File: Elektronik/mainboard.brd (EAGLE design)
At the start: 27 x 27.4 mm, 35 parts, among them IC1 TXS0102DCU, IC2 SP6201EM5-L-3-3, IC3 SRV05-4.TCT, X2 USB-MINI32005-601, X4 MICROMATCH-8-WEIBLICH

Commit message: [Elektronik] Spannungsteiler für VBUS angepasst, damit die Pullups der Datenleitungen die VBUS-leitung nicht über die ESD-Dioden nach oben ziehen
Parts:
- R1: value 27k -> 2k7
- R2: value 47k -> 4k7
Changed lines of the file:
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@@
 <attribute name="WUERTH" value="824001" x="4.8" y="5.6" size="1.778" layer="28" rot="MR90" display="off"/>
 </element>
-<element name="R1" library="rcl" package="R0603" value="27k" x="10.4" y="5.4" rot="MR90"/>
-<element name="R2" library="rcl" package="R0603" value="47k" x="10.4" y="2.4" rot="MR90"/>
+<element name="R1" library="rcl" package="R0603" value="2k7" x="10.4" y="5.4" rot="MR90"/>
+<element name="R2" library="rcl" package="R0603" value="4k7" x="10.4" y="2.4" rot="MR90"/>
 <element name="R3" library="rcl" package="R0603" value="1M" x="1.6" y="9" rot="MR90"/>
 <element name="C11" library="rcl" package="C0603" value="4n7" x="1.6" y="5.8" rot="MR90"/>

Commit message: Items sind jetzt alle selectable
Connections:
- net /RESET renamed !RESET!
- net /TASTER1 renamed !TASTER1!
- net /TASTER2 renamed !TASTER2!
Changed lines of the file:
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@@
 <wire x1="10.4" y1="4.55" x2="10.4" y2="3.25" width="0.2" layer="16"/>
 </signal>
-<signal name="/RESET">
+<signal name="!RESET!">
 <contactref element="U$1" pad="57"/>
 <contactref element="TA1" pad="1"/>
@@
 <wire x1="16.25" y1="17.4" x2="17.6" y2="17.4" width="0.3" layer="1"/>
 </signal>
-<signal name="/TASTER1">
+<signal name="!TASTER1!">
 <contactref element="TA2" pad="1"/>
 <contactref element="R5" pad="1"/>
@@
 <wire x1="4.3962" y1="14.4" x2="4.4403" y2="14.4441" width="0.3" layer="16"/>
 </signal>
-<signal name="/TASTER2">
+<signal name="!TASTER2!">
 <contactref element="TA3" pad="1"/>
 <contactref element="R6" pad="1"/>

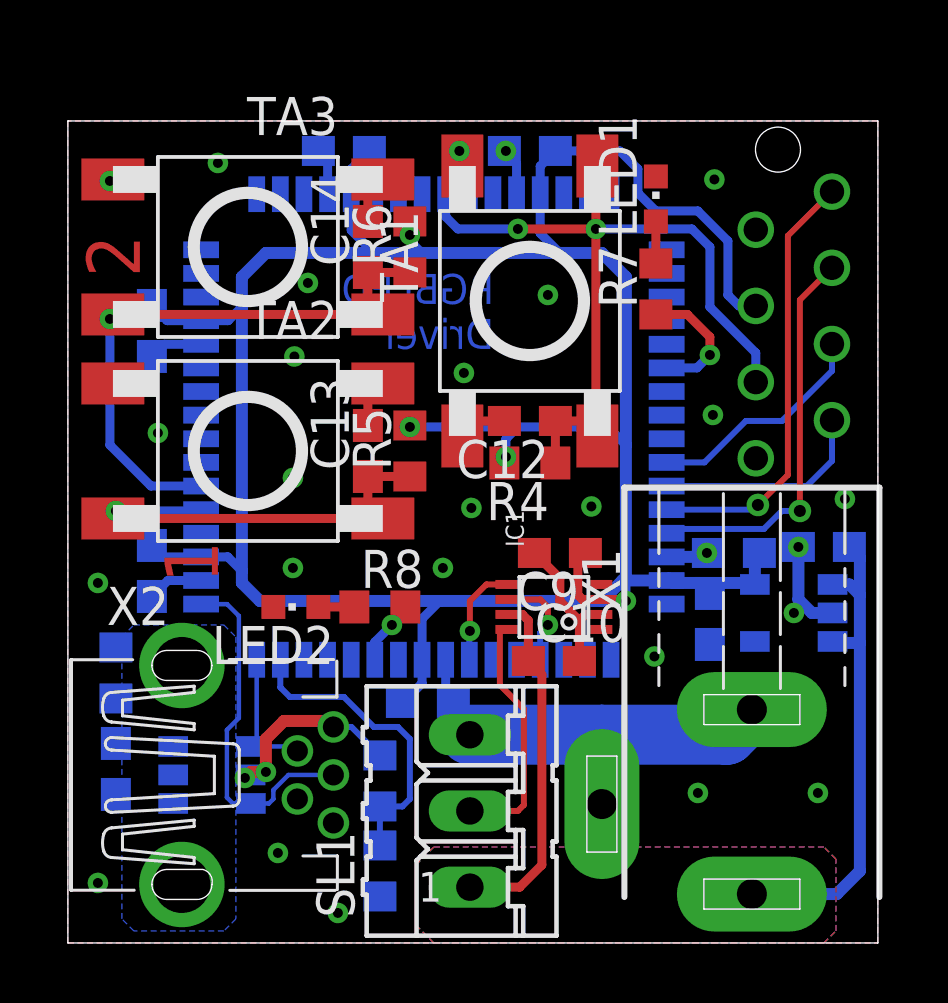
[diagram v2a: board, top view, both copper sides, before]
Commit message: [Elektronik] Layout für Fertigung in der Uni angepasst
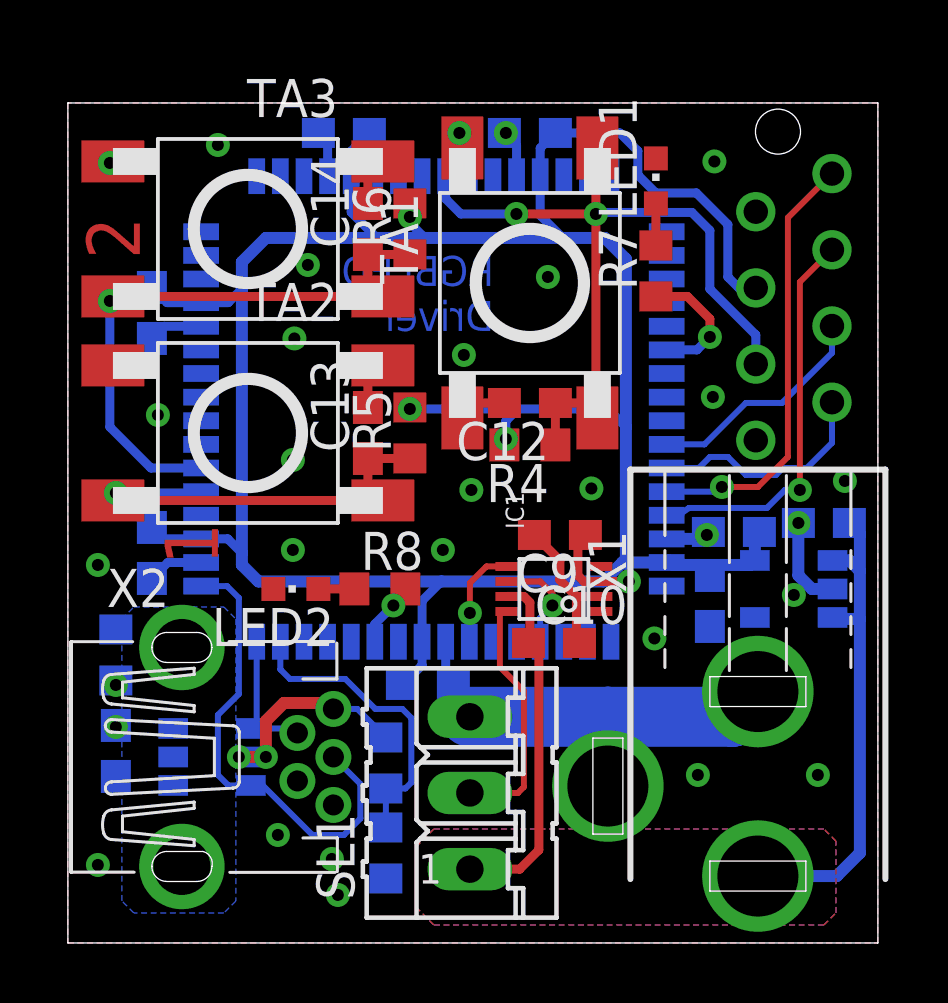
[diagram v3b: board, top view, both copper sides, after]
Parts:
- moved C1 0.80 mm to (25.2, 14.0)
- moved IC2 0.80 mm to (24.2, 11.8)
- moved C3 0.70 mm to (22.2, 13.7)
- moved X1 0.63 mm to (23.0, 10.8)
- moved R2 0.63 mm to (10.6, 3.00)
- moved R1 0.63 mm to (10.6, 6.00)
- moved C12 0.60 mm to (15.4, 18.0)
- moved C13 0.60 mm to (10.0, 17.0)
- moved C14 0.60 mm to (10.0, 23.8)
- moved C6 0.60 mm to (2.80, 21.0)
- moved C7 0.60 mm to (9.20, 27.0)
- moved C8 0.60 mm to (15.4, 27.0)
- moved IC1 0.60 mm to (16.2, 11.8)
- moved LED2 0.60 mm to (7.60, 11.8)
- moved R4 0.60 mm to (15.4, 16.6)
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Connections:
- net USB_N renamed USB_DM
- net USB_P renamed USB_DP
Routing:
- net USB_DP: track 11.8 -> 15.8 mm
- net VBUS: track 7.42 -> 8.11 mm
- net GND: vias 27 -> 30
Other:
- board size 27 x 27.4 mm -> 27 x 28 mm
